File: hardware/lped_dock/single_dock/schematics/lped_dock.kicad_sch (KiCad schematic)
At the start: 1 part

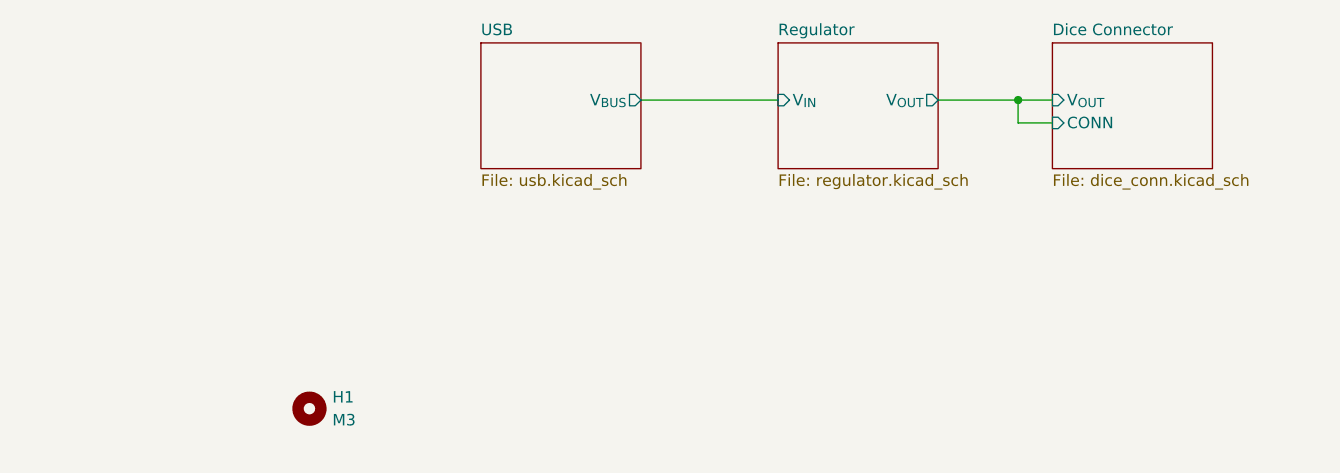
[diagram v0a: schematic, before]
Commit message: feat(hardware): add battery charger and connector to single charger
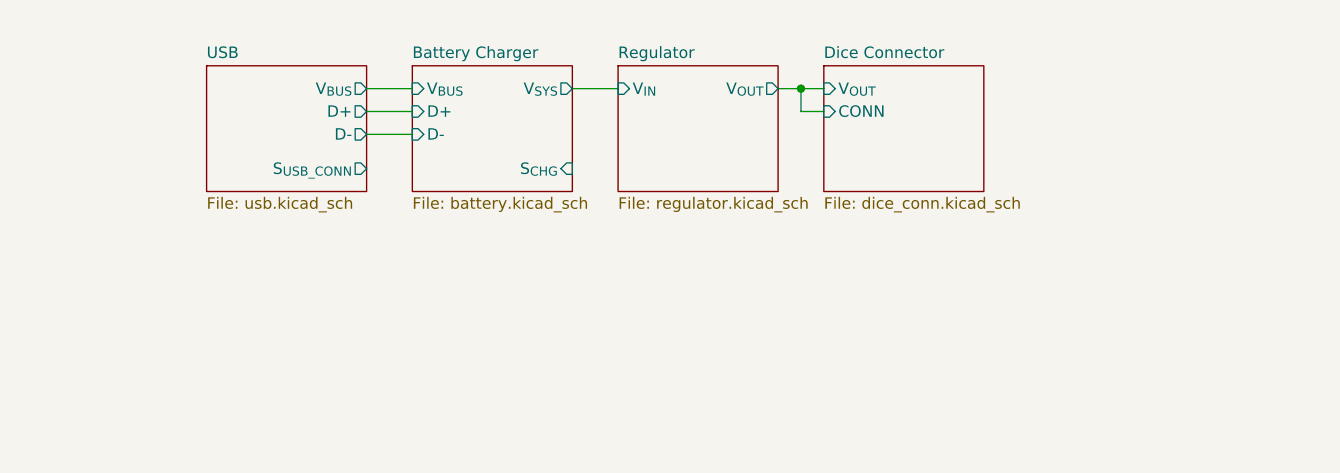
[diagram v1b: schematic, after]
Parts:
- removed H1: M3, MountingHole:MountingHole_3.2mm_M3_DIN965_Pad, symbol Mechanical:MountingHole
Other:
- added sheet Battery Charger (battery.kicad_sch)
- sheet USB ports: added D+, D-, S_{USB_CONN}; removed none
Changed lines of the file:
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@@
 	)
 	(junction
-		(at 152.4 83.82)
+		(at 128.27 82.55)
 		(diameter 0)
 		(color 0 0 0 0)
@@
 	(wire
 		(pts
-			(xy 152.4 83.82) (xy 156.21 83.82)
-		)
-		(stroke
-			(width 0)
-			(type default)
-		)
-	)
-	(wire
-		(pts
-			(xy 152.4 86.36) (xy 156.21 86.36)
-		)
-		(stroke
-			(width 0)
-			(type default)
-		)
-	)
-	(wire
-		(pts
-			(xy 152.4 83.82) (xy 152.4 86.36)
-		)
-		(stroke
-			(width 0)
-			(type default)
-		)
-	)
-	(wire
-		(pts
-			(xy 143.51 83.82) (xy 152.4 83.82)
-		)
-		(stroke
-			(width 0)
-			(type default)
-		)
-	)
-	(wire
-		(pts
-			(xy 110.49 83.82) (xy 125.73 83.82)
-		)
-		(stroke
-			(width 0)
-			(type default)
-		)
-	)
-	(symbol
-		(lib_id "Mechanical:MountingHole")
-		(at 73.66 118.11 0)
-		(unit 1)
-		(exclude_from_sim yes)
-		(in_bom no)
-		(on_board yes)
-		(dnp no)
-		(fields_autoplaced yes)
-		(property "Reference" "H1"
-			(at 76.2 116.84 0)
-			(effects
-				(font
-					(size 1.27 1.27)
-				)
-				(justify left)
-			)
-		)
-		(property "Value" "M3"
-			(at 76.2 119.38 0)
-			(effects
-				(font
-					(size 1.27 1.27)
-				)
-				(justify left)
-			)
-		)
-		(property "Footprint" "MountingHole:MountingHole_3.2mm_M3_DIN965_Pad"
-			(at 73.66 118.11 0)
-			(effects
-				(font
-					(size 1.27 1.27)
-				)
-				(hide yes)
-			)
-		)
-		(property "Datasheet" "~"
-			(at 73.66 118.11 0)
-			(effects
-				(font
-					(size 1.27 1.27)
-				)
-				(hide yes)
-			)
-		)
-		(property "Description" "Mounting Hole without connection"
-			(at 73.66 118.11 0)
-			(effects
-				(font
-					(size 1.27 1.27)
-				)
-				(hide yes)
-			)
-		)
-		(instances
-			(project ""
-				(path "/5c78e66f-0328-4fd7-bcaa-ded4a2671f1d"
-					(reference "H1")
-					(unit 1)
-				)
-			)
+			(xy 128.27 85.09) (xy 130.81 85.09)
+		)
+		(stroke
+			(width 0)
+			(type default)
+		)
+	)
+	(wire
+		(pts
+			(xy 80.01 82.55) (xy 85.09 82.55)
+		)
+		(stroke
+			(width 0)
+			(type default)
+		)
+	)
+	(wire
+		(pts
+			(xy 125.73 82.55) (xy 128.27 82.55)
+		)
+		(stroke
+			(width 0)
+			(type default)
+		)
+	)
+	(wire
+		(pts
+			(xy 80.01 85.09) (xy 85.09 85.09)
+		)
+		(stroke
+			(width 0)
+			(type default)
+		)
+	)
+	(wire
+		(pts
+			(xy 80.01 87.63) (xy 85.09 87.63)
+		)
+		(stroke
+			(width 0)
+			(type default)
+		)
+	)
+	(wire
+		(pts
+			(xy 102.87 82.55) (xy 107.95 82.55)
+		)
+		(stroke
+			(width 0)
+			(type default)
+		)
+	)
+	(wire
+		(pts
+			(xy 128.27 82.55) (xy 130.81 82.55)
+		)
+		(stroke
+			(width 0)
+			(type default)
+		)
+	)
+	(wire
+		(pts
+			(xy 128.27 82.55) (xy 128.27 85.09)
+		)
+		(stroke
+			(width 0)
+			(type default)
 		)
 	)
 	(sheet
-		(at 125.73 77.47)
+		(at 107.95 80.01)
 		(size 17.78 13.97)
 		(exclude_from_sim no)
@@
 		)
 		(property "Sheetname" "Regulator"
-			(at 125.73 76.7584 0)
+			(at 107.95 79.2984 0)
 			(effects
 				(font
@@
 		)
 		(property "Sheetfile" "regulator.kicad_sch"
-			(at 125.73 92.0246 0)
+			(at 107.95 94.5646 0)
 			(effects
 				(font
@@
 		)
 		(pin "V_{IN}" input
-			(at 125.73 83.82 180)
+			(at 107.95 82.55 180)
 			(effects
 				(font
@@
 		)
 		(pin "V_{OUT}" output
-			(at 143.51 83.82 0)
+			(at 125.73 82.55 0)
 			(effects
 				(font
@@
 			(project "lped_dock"
 				(path "/5c78e66f-0328-4fd7-bcaa-ded4a2671f1d"
-					(page "3")
+					(page "4")
 				)
 			)
@@
 	)
 	(sheet
-		(at 156.21 77.47)
+		(at 130.81 80.01)
 		(size 17.78 13.97)
 		(exclude_from_sim no)
@@
 		)
 		(property "Sheetname" "Dice Connector"
-			(at 156.21 76.7584 0)
+			(at 130.81 79.2984 0)
 			(effects
 				(font
@@
 		)
 		(property "Sheetfile" "dice_conn.kicad_sch"
-			(at 156.21 92.0246 0)
+			(at 130.81 94.5646 0)
 			(effects
 				(font
@@
 		)
 		(pin "CONN" input
-			(at 156.21 86.36 180)
+			(at 130.81 85.09 180)
 			(effects
 				(font
@@
 		)
 		(pin "V_{OUT}" input
-			(at 156.21 83.82 180)
+			(at 130.81 82.55 180)
 			(effects
 				(font
@@
 			(project "lped_dock"
 				(path "/5c78e66f-0328-4fd7-bcaa-ded4a2671f1d"
-					(page "4")
+					(page "5")
 				)
 			)
@@
 	)
 	(sheet
-		(at 92.71 77.47)
+		(at 62.23 80.01)
 		(size 17.78 13.97)
 		(exclude_from_sim no)
@@
 		)
 		(property "Sheetname" "USB"
-			(at 92.71 76.7584 0)
+			(at 62.23 79.2984 0)
 			(effects
 				(font
@@
 		)
 		(property "Sheetfile" "usb.kicad_sch"
-			(at 92.71 92.0246 0)
+			(at 62.23 94.5646 0)
 			(effects
 				(font
@@
 		)
 		(pin "V_{BUS}" output
-			(at 110.49 83.82 0)
-			(effects
-				(font
+			(at 80.01 82.55 0)
+			(effects
+				(font
+					(size 1.27 1.27)
+				)
+				(justify right)
+			)
+		)
+		(pin "D+" output
+			(at 80.01 85.09 0)
+			(effects
+				(font
+					(size 1.27 1.27)
+				)
+				(justify right)
+			)
+		)
+		(pin "D-" output
+			(at 80.01 87.63 0)
+			(effects
+				(font
+					(size 1.27 1.27)
+				)
+				(justify right)
+			)
+		)
+		(pin "S_{USB_CONN}" output
+			(at 80.01 91.44 0)
+			(effects
+				(font
+					(size 1.27 1.27)
+				)
+				(justify right)
+			)
+		)
+		(instances
+			(project "lped_dock"
+				(path "/5c78e66f-0328-4fd7-bcaa-ded4a2671f1d"
+					(page "2")
+				)
+			)
+		)
+	)
+	(sheet
+		(at 85.09 80.01)
+		(size 17.78 13.97)
+		(exclude_from_sim no)
+		(in_bom yes)
+		(on_board yes)
+		(dnp no)
+		(fields_autoplaced yes)
+		(stroke
+			(width 0.1524)
+			(type solid)
+		)
+		(fill
+			(color 0 0 0 0.0000)
+		)
+		(property "Sheetname" "Battery Charger"
+			(at 85.09 79.2984 0)
+			(effects
+				(font
+					(size 1.27 1.27)
+				)
+				(justify left bottom)
+			)
+		)
+		(property "Sheetfile" "battery.kicad_sch"
+			(at 85.09 94.5646 0)
+			(effects
+				(font
+					(size 1.27 1.27)
+				)
+				(justify left top)
+			)
+		)
+		(pin "D+" input
+			(at 85.09 85.09 180)
+			(effects
+				(font
+					(size 1.27 1.27)
+				)
+				(justify left)
+			)
+		)
+		(pin "D-" input
+			(at 85.09 87.63 180)
+			(effects
+				(font
+					(size 1.27 1.27)
+				)
+				(justify left)
+			)
+		)
+		(pin "S_{CHG}" input
+			(at 102.87 91.44 0)
+			(effects
+				(font
+					(size 1.27 1.27)
+				)
+				(justify right)
+			)
+		)
+		(pin "V_{BUS}" input
+			(at 85.09 82.55 180)
+			(effects
+				(font
+					(size 1.27 1.27)
+				)
+				(justify left)
+			)
+		)
+		(pin "V_{SYS}" output
+			(at 102.87 82.55 0)
+			(effects
+				(font

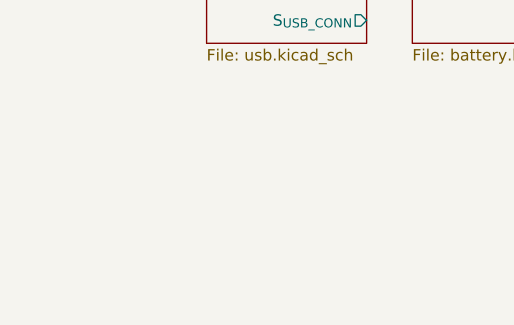
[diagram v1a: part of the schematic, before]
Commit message: feat(hardware): change regulator, add mounting hole to single charger
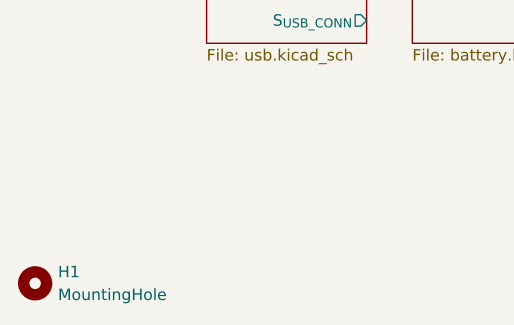
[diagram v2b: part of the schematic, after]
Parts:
- added H1: MountingHole, symbol Mechanical:MountingHole
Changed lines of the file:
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@@
+		)
+	)
+	(symbol
+		(lib_id "Mechanical:MountingHole")
+		(at 43.18 120.65 0)
+		(unit 1)
+		(exclude_from_sim no)
+		(in_bom no)
+		(on_board yes)
+		(dnp no)
+		(fields_autoplaced yes)
+		(property "Reference" "H1"
+			(at 45.72 119.3799 0)
+			(effects
+				(font
+					(size 1.27 1.27)
+				)
+				(justify left)
+			)
+		)
+		(property "Value" "MountingHole"
+			(at 45.72 121.9199 0)
+			(effects
+				(font
+					(size 1.27 1.27)
+				)
+				(justify left)
+			)
+		)
+		(property "Footprint" ""
+			(at 43.18 120.65 0)
+			(effects
+				(font
+					(size 1.27 1.27)
+				)
+				(hide yes)
+			)
+		)
+		(property "Datasheet" "~"
+			(at 43.18 120.65 0)
+			(effects
+				(font
+					(size 1.27 1.27)
+				)
+				(hide yes)
+			)
+		)
+		(property "Description" "Mounting Hole without connection"
+			(at 43.18 120.65 0)
+			(effects
+				(font
+					(size 1.27 1.27)
+				)
+				(hide yes)
+			)
+		)
+		(instances
+			(project ""
+				(path "/5c78e66f-0328-4fd7-bcaa-ded4a2671f1d"
+					(reference "H1")
+					(unit 1)
+				)
+			)
 		)
 	)

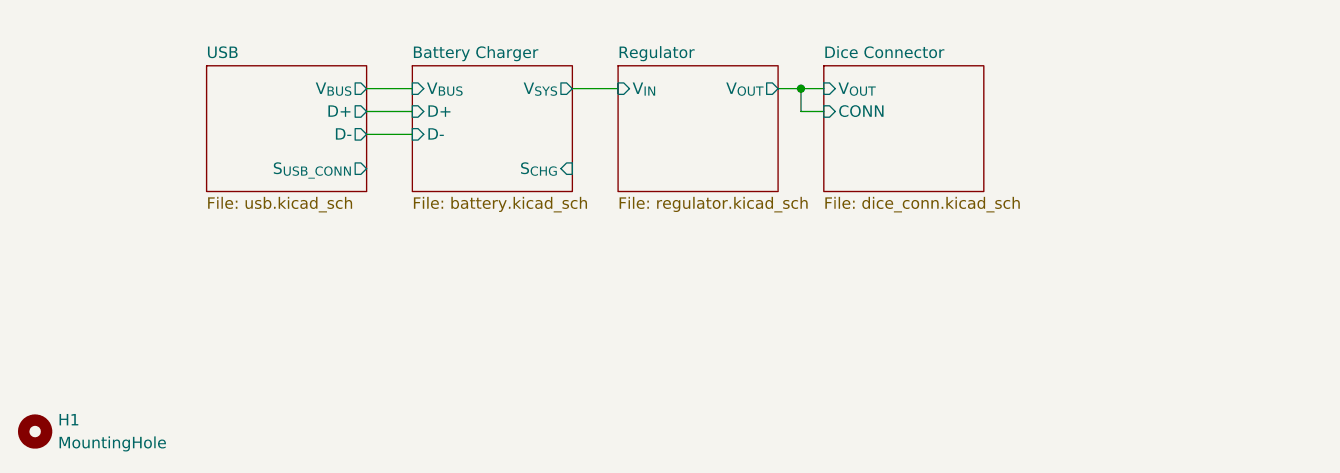
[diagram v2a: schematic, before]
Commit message: feat(hardware): improvements to dock battery system
* Added current limiting resistor to battery
* Added charging status LED
* Changed side of battery connector
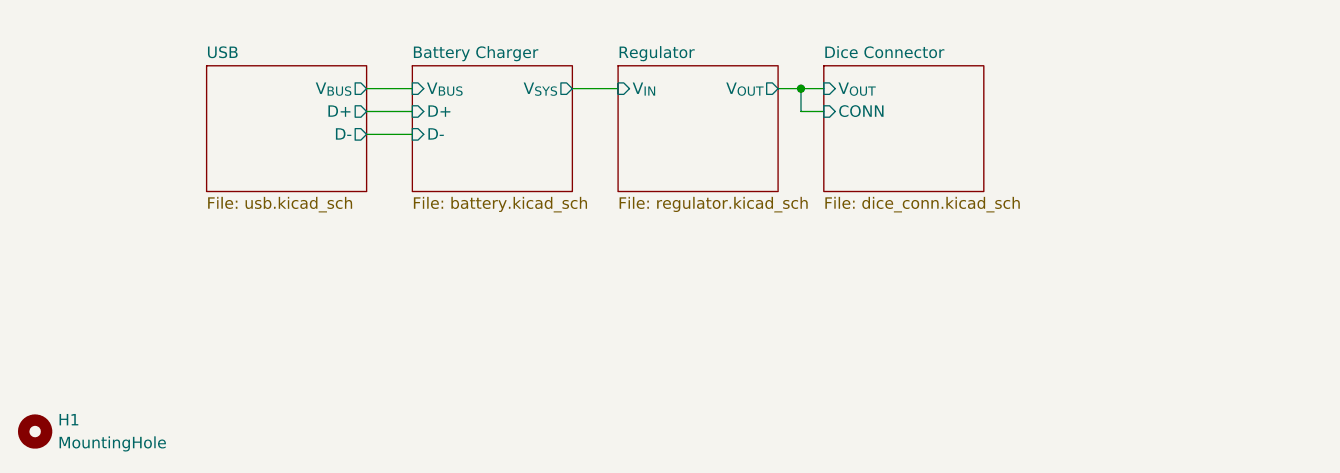
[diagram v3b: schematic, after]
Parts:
- H1: footprint (none) -> MountingHole:MountingHole_3.2mm_M3
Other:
- sheet Battery Charger ports: added none; removed S_{CHG}
- sheet USB ports: added none; removed S_{USB_CONN}
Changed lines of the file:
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@@
 			)
 		)
-		(property "Footprint" ""
+		(property "Footprint" "MountingHole:MountingHole_3.2mm_M3"
 			(at 43.18 120.65 0)
 			(effects
@@
 			)
 		)
-		(pin "S_{USB_CONN}" output
-			(at 80.01 91.44 0)
-			(effects
-				(font
-					(size 1.27 1.27)
-				)
-				(justify right)
-			)
-		)
 		(instances
 			(project "lped_dock"
@@
 			)
 		)
-		(pin "S_{CHG}" input
-			(at 102.87 91.44 0)
-			(effects
-				(font
-					(size 1.27 1.27)
-				)
-				(justify right)
-			)
-		)

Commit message: feat(hardware): add batt charger bypass solder jump
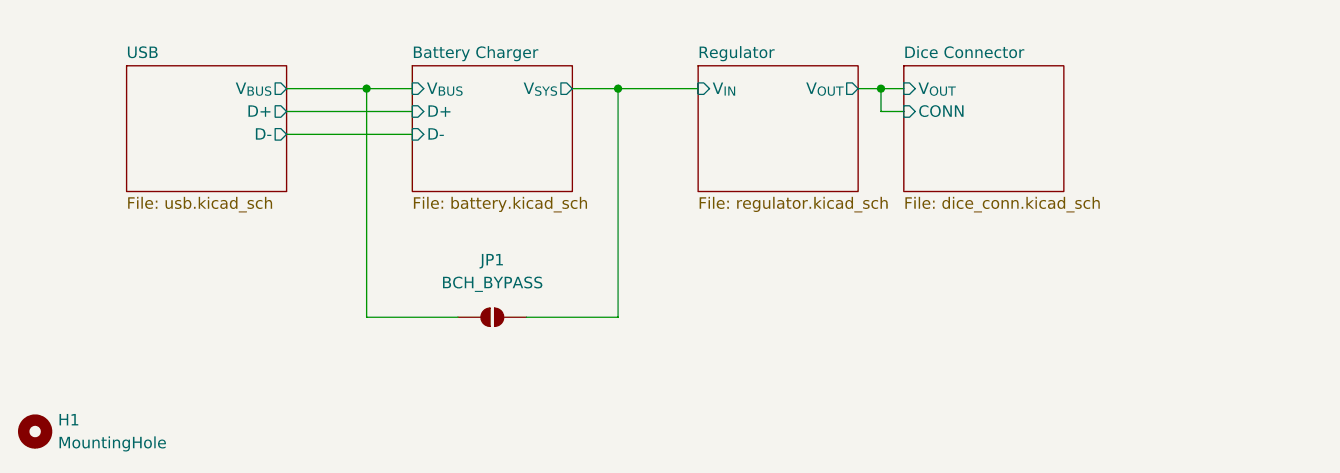
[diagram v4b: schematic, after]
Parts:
- added JP1: BCH_BYPASS, Jumper:SolderJumper-2_P1.3mm_Open_Pad1.0x1.5mm, symbol Jumper:SolderJumper_2_Open
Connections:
- net Battery Charger/V_{BUS}: now also JP1.1 (A)
- net Battery Charger/V_{SYS}: now also JP1.2 (B)
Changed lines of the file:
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@@
 	)
 	(junction
-		(at 128.27 82.55)
+		(at 80.01 82.55)
 		(diameter 0)
 		(color 0 0 0 0)
 	)
-	(wire
-		(pts
-			(xy 128.27 85.09) (xy 130.81 85.09)
+	(junction
+		(at 107.95 82.55)
+		(diameter 0)
+		(color 0 0 0 0)
+	)
+	(junction
+		(at 137.16 82.55)
+		(diameter 0)
+		(color 0 0 0 0)
+	)
+	(wire
+		(pts
+			(xy 107.95 107.95) (xy 107.95 82.55)
 		)
 		(stroke
@@
 	(wire
 		(pts
-			(xy 125.73 82.55) (xy 128.27 82.55)
-		)
-		(stroke
-			(width 0)
-			(type default)
-		)
-	)
-	(wire
-		(pts
-			(xy 80.01 85.09) (xy 85.09 85.09)
-		)
-		(stroke
-			(width 0)
-			(type default)
-		)
-	)
-	(wire
-		(pts
-			(xy 80.01 87.63) (xy 85.09 87.63)
+			(xy 137.16 85.09) (xy 139.7 85.09)
+		)
+		(stroke
+			(width 0)
+			(type default)
+		)
+	)
+	(wire
+		(pts
+			(xy 71.12 82.55) (xy 80.01 82.55)
+		)
+		(stroke
+			(width 0)
+			(type default)
+		)
+	)
+	(wire
+		(pts
+			(xy 134.62 82.55) (xy 137.16 82.55)
+		)
+		(stroke
+			(width 0)
+			(type default)
+		)
+	)
+	(wire
+		(pts
+			(xy 71.12 85.09) (xy 85.09 85.09)
+		)
+		(stroke
+			(width 0)
+			(type default)
+		)
+	)
+	(wire
+		(pts
+			(xy 71.12 87.63) (xy 85.09 87.63)
 		)
 		(stroke
@@
 	(wire
 		(pts
-			(xy 128.27 82.55) (xy 130.81 82.55)
-		)
-		(stroke
-			(width 0)
-			(type default)
-		)
-	)
-	(wire
-		(pts
-			(xy 128.27 82.55) (xy 128.27 85.09)
+			(xy 80.01 107.95) (xy 90.17 107.95)
+		)
+		(stroke
+			(width 0)
+			(type default)
+		)
+	)
+	(wire
+		(pts
+			(xy 137.16 82.55) (xy 139.7 82.55)
+		)
+		(stroke
+			(width 0)
+			(type default)
+		)
+	)
+	(wire
+		(pts
+			(xy 137.16 82.55) (xy 137.16 85.09)
+		)
+		(stroke
+			(width 0)
+			(type default)
+		)
+	)
+	(wire
+		(pts
+			(xy 107.95 82.55) (xy 116.84 82.55)
+		)
+		(stroke
+			(width 0)
+			(type default)
+		)
+	)
+	(wire
+		(pts
+			(xy 80.01 82.55) (xy 80.01 107.95)
+		)
+		(stroke
+			(width 0)
+			(type default)
+		)
+	)
+	(wire
+		(pts
+			(xy 97.79 107.95) (xy 107.95 107.95)
 		)
 		(stroke
@@
 		)
 	)
+	(symbol
+		(lib_id "Jumper:SolderJumper_2_Open")
+		(at 93.98 107.95 0)
+		(unit 1)
+		(exclude_from_sim no)
+		(in_bom no)
+		(on_board yes)
+		(dnp no)
+		(fields_autoplaced yes)
+		(property "Reference" "JP1"
+			(at 93.98 101.6 0)
+			(effects
+				(font
+					(size 1.27 1.27)
+				)
+			)
+		)
+		(property "Value" "BCH_BYPASS"
+			(at 93.98 104.14 0)
+			(effects
+				(font
+					(size 1.27 1.27)
+				)
+			)
+		)
+		(property "Footprint" "Jumper:SolderJumper-2_P1.3mm_Open_Pad1.0x1.5mm"
+			(at 93.98 107.95 0)
+			(effects
+				(font
+					(size 1.27 1.27)
+				)
+				(hide yes)
+			)
+		)
+		(property "Datasheet" "~"
+			(at 93.98 107.95 0)
+			(effects
+				(font
+					(size 1.27 1.27)
+				)
+				(hide yes)
+			)
+		)
+		(property "Description" "Solder Jumper, 2-pole, open"
+			(at 93.98 107.95 0)
+			(effects
+				(font
+					(size 1.27 1.27)
+				)
+				(hide yes)
+			)
+		)
+		(pin "2"
+		)
+		(pin "1"
+		)
+		(instances
+			(project ""
+				(path "/5c78e66f-0328-4fd7-bcaa-ded4a2671f1d"
+					(reference "JP1")
+					(unit 1)
+				)
+			)
+		)
+	)
 	(sheet
-		(at 107.95 80.01)
+		(at 116.84 80.01)
 		(size 17.78 13.97)
 		(exclude_from_sim no)
@@
 		)
 		(property "Sheetname" "Regulator"
-			(at 107.95 79.2984 0)
+			(at 116.84 79.2984 0)
 			(effects
 				(font
@@
 		)
 		(property "Sheetfile" "regulator.kicad_sch"
-			(at 107.95 94.5646 0)
+			(at 116.84 94.5646 0)
 			(effects
 				(font
@@
 		)
 		(pin "V_{IN}" input
-			(at 107.95 82.55 180)
+			(at 116.84 82.55 180)
 			(effects
 				(font
@@
 		)
 		(pin "V_{OUT}" output
-			(at 125.73 82.55 0)
+			(at 134.62 82.55 0)
 			(effects
 				(font
@@
 	)
 	(sheet
-		(at 130.81 80.01)
+		(at 139.7 80.01)
 		(size 17.78 13.97)
 		(exclude_from_sim no)
@@
 		)
 		(property "Sheetname" "Dice Connector"
-			(at 130.81 79.2984 0)
+			(at 139.7 79.2984 0)
 			(effects
 				(font
@@
 		)
 		(property "Sheetfile" "dice_conn.kicad_sch"
-			(at 130.81 94.5646 0)
+			(at 139.7 94.5646 0)
 			(effects
 				(font
@@
 		)
 		(pin "CONN" input
-			(at 130.81 85.09 180)
+			(at 139.7 85.09 180)
 			(effects
 				(font
@@
 		)
 		(pin "V_{OUT}" input
-			(at 130.81 82.55 180)
+			(at 139.7 82.55 180)
 			(effects
 				(font
@@
 	)
 	(sheet
-		(at 62.23 80.01)
+		(at 53.34 80.01)
 		(size 17.78 13.97)
 		(exclude_from_sim no)
@@
 		)
 		(property "Sheetname" "USB"
-			(at 62.23 79.2984 0)
+			(at 53.34 79.2984 0)
 			(effects
 				(font
@@
 		)
 		(property "Sheetfile" "usb.kicad_sch"
-			(at 62.23 94.5646 0)
+			(at 53.34 94.5646 0)
 			(effects
 				(font
@@
 		)
 		(pin "V_{BUS}" output
-			(at 80.01 82.55 0)
+			(at 71.12 82.55 0)
 			(effects
 				(font
@@
 		)
 		(pin "D+" output
-			(at 80.01 85.09 0)
+			(at 71.12 85.09 0)
 			(effects
 				(font
@@
 		)
 		(pin "D-" output
-			(at 80.01 87.63 0)
-			(effects
-				(font
+			(at 71.12 87.63 0)
+			(effects
+				(font
